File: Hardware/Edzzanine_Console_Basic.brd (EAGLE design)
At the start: 30.5 x 44.5 mm, 29 parts, among them U4 TPS62065

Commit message: fixed rx tx
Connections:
- net N$1 renamed RXD
- net N$2 renamed TXD
- net N$3: now also R7.1; no longer R6.1
- net N$4: now also R6.1; no longer R7.1
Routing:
- net N$4: track 9.96 -> 10.9 mm
- net N$3: track 11.4 -> 11.2 mm, vias 2 -> 0
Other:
- board text added: "BLK"
- board text added: "GRN"
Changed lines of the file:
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@@
 <setting verticaltext="up"/>
 </settings>
-<grid distance="0.01" unitdist="inch" unit="inch" style="lines" multiple="1" display="yes" altdistance="0.005" altunitdist="inch" altunit="inch"/>
+<grid distance="0.005" unitdist="inch" unit="inch" style="lines" multiple="1" display="yes" altdistance="0.005" altunitdist="inch" altunit="inch"/>
 <layers>
 <layer number="1" name="Top" color="4" fill="1" visible="yes" active="yes"/>
@@
 <text x="30.099" y="3.81" size="1.016" layer="1" font="vector" ratio="15" rot="R90">v01</text>
 <text x="28.956" y="32.258" size="1.27" layer="21" font="vector" ratio="15" rot="R90" align="center">Console Basic</text>
+<text x="6.731" y="39.878" size="1.27" layer="21" font="vector" ratio="15" rot="R90" align="center-right">GRN</text>
+<text x="23.749" y="39.878" size="1.27" layer="21" font="vector" ratio="15" rot="R90" align="center-right">BLK</text>
 </plain>
 <attributes>
@@
 <wire x1="11.176" y1="18.542" x2="9.888" y2="18.542" width="0.254" layer="1"/>
 </signal>
-<signal name="N$1">
+<signal name="RXD">
 <contactref element="U1" pad="13"/>
 <contactref element="JP2" pad="5"/>
@@
 <wire x1="11.43" y1="33.354" x2="11.43" y2="30.48" width="0.254" layer="1"/>
 </signal>
-<signal name="N$2">
+<signal name="TXD">
 <contactref element="U1" pad="12"/>
 <contactref element="JP2" pad="4"/>
@@
 <signal name="N$3">
 <contactref element="U1" pad="2"/>
-<contactref element="R6" pad="1"/>
-<wire x1="18.708" y1="24.384" x2="17.018" y2="24.384" width="0.1524" layer="1"/>
-<via x="17.018" y="24.384" extent="1-16" drill="0.508"/>
-<wire x1="17.018" y1="24.384" x2="14.478" y2="24.384" width="0.1524" layer="16"/>
-<wire x1="14.478" y1="24.384" x2="12.192" y2="26.67" width="0.1524" layer="16"/>
-<wire x1="12.192" y1="26.67" x2="12.192" y2="27.432" width="0.1524" layer="16"/>
-<wire x1="12.192" y1="27.432" x2="11.176" y2="28.448" width="0.1524" layer="16"/>
-<via x="11.176" y="28.448" extent="1-16" drill="0.508"/>
-<wire x1="11.176" y1="28.448" x2="10.668" y2="28.956" width="0.1524" layer="1"/>
-<wire x1="10.668" y1="28.956" x2="9.646" y2="28.956" width="0.1524" layer="1"/>
+<contactref element="R7" pad="1"/>
+<wire x1="18.708" y1="26.035" x2="17.526" y2="26.035" width="0.1778" layer="1"/>
+<wire x1="17.526" y1="26.035" x2="17.272" y2="25.781" width="0.1778" layer="1"/>
+<wire x1="17.272" y1="25.781" x2="13.081" y2="25.781" width="0.1778" layer="1"/>
+<wire x1="13.081" y1="25.781" x2="12.192" y2="26.67" width="0.1778" layer="1"/>
+<wire x1="12.192" y1="26.67" x2="12.192" y2="27.94" width="0.1778" layer="1"/>
+<wire x1="12.192" y1="27.94" x2="11.176" y2="28.956" width="0.1778" layer="1"/>
+<wire x1="11.176" y1="28.956" x2="9.646" y2="28.956" width="0.1778" layer="1"/>
 </signal>
 <signal name="N$4">
 <contactref element="U1" pad="3"/>
-<contactref element="R7" pad="1"/>
-<wire x1="18.708" y1="26.035" x2="18.454" y2="25.781" width="0.1524" layer="1"/>
-<wire x1="18.454" y1="25.781" x2="13.081" y2="25.781" width="0.1524" layer="1"/>
-<wire x1="13.081" y1="25.781" x2="11.176" y2="27.686" width="0.1524" layer="1"/>
-<wire x1="11.176" y1="27.686" x2="9.646" y2="27.686" width="0.1524" layer="1"/>
+<contactref element="R6" pad="1"/>
+<wire x1="18.708" y1="24.384" x2="18.581" y2="24.511" width="0.1778" layer="1"/>
+<wire x1="18.581" y1="24.511" x2="13.716" y2="24.511" width="0.1778" layer="1"/>
+<wire x1="13.716" y1="24.511" x2="11.811" y2="26.416" width="0.1778" layer="1"/>
+<wire x1="11.811" y1="26.416" x2="11.811" y2="27.178" width="0.1778" layer="1"/>
+<wire x1="11.811" y1="27.178" x2="11.303" y2="27.686" width="0.1778" layer="1"/>
+<wire x1="11.303" y1="27.686" x2="9.646" y2="27.686" width="0.1778" layer="1"/>
 </signal>
 </signals>

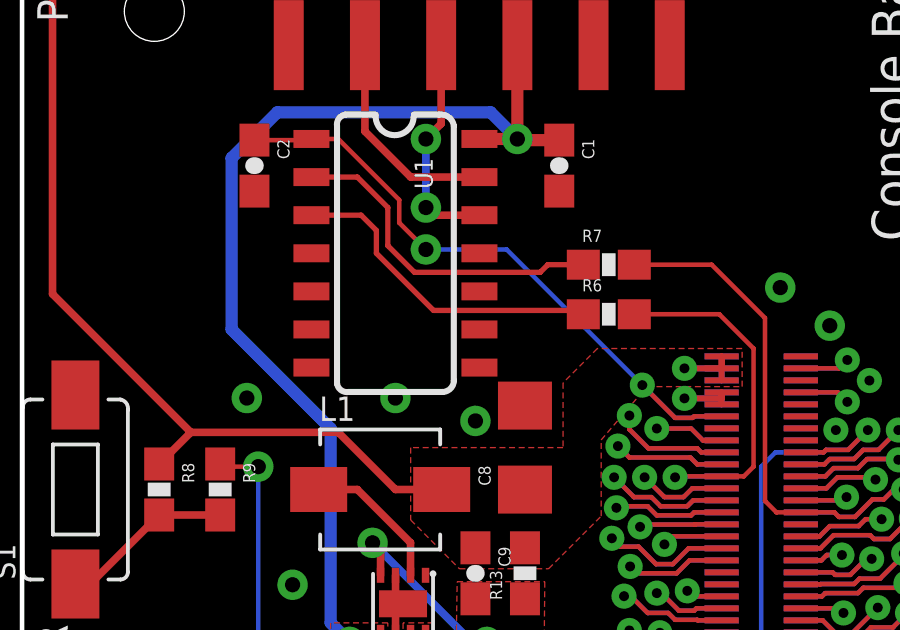
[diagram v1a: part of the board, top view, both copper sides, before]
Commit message: fixed OE to high
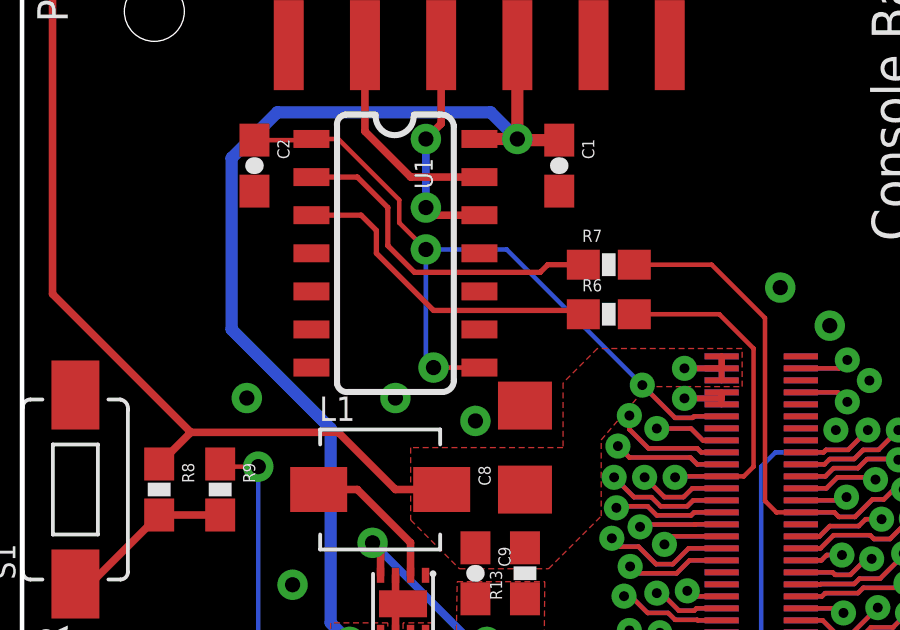
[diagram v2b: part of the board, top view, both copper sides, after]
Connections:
- net 1.8V: now also U1.8
- net GND: no longer U1.8
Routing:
- net 1.8V: track 23.0 -> 28.6 mm, vias 2 -> 3
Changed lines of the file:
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@@
 <contactref element="R14" pad="1"/>
 <contactref element="U1" pad="7"/>
-<contactref element="U1" pad="8"/>
 <wire x1="12.45" y1="13.782" x2="12.45" y2="14.482" width="0.254" layer="1"/>
 <wire x1="12.45" y1="14.482" x2="12.7" y2="14.732" width="0.254" layer="1"/>
@@
 <wire x1="9.646" y1="30.226" x2="9.607" y2="30.187" width="0.1524" layer="1"/>
 <wire x1="9.607" y1="30.187" x2="7.747" y2="30.187" width="0.1524" layer="1"/>
+<contactref element="U1" pad="8"/>
+<wire x1="15.246" y1="22.606" x2="13.716" y2="22.606" width="0.1524" layer="1"/>
+<via x="13.716" y="22.606" extent="1-16" drill="0.508"/>
+<wire x1="13.716" y1="22.606" x2="13.462" y2="22.86" width="0.1524" layer="16"/>
+<wire x1="13.462" y1="22.86" x2="13.462" y2="26.543" width="0.1524" layer="16"/>
 </signal>
 <signal name="FW_RCVR">
